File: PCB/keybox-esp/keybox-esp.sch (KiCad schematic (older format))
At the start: 3 parts, among them J1 Micro_SD_Card, U1 ESP32-WROVER

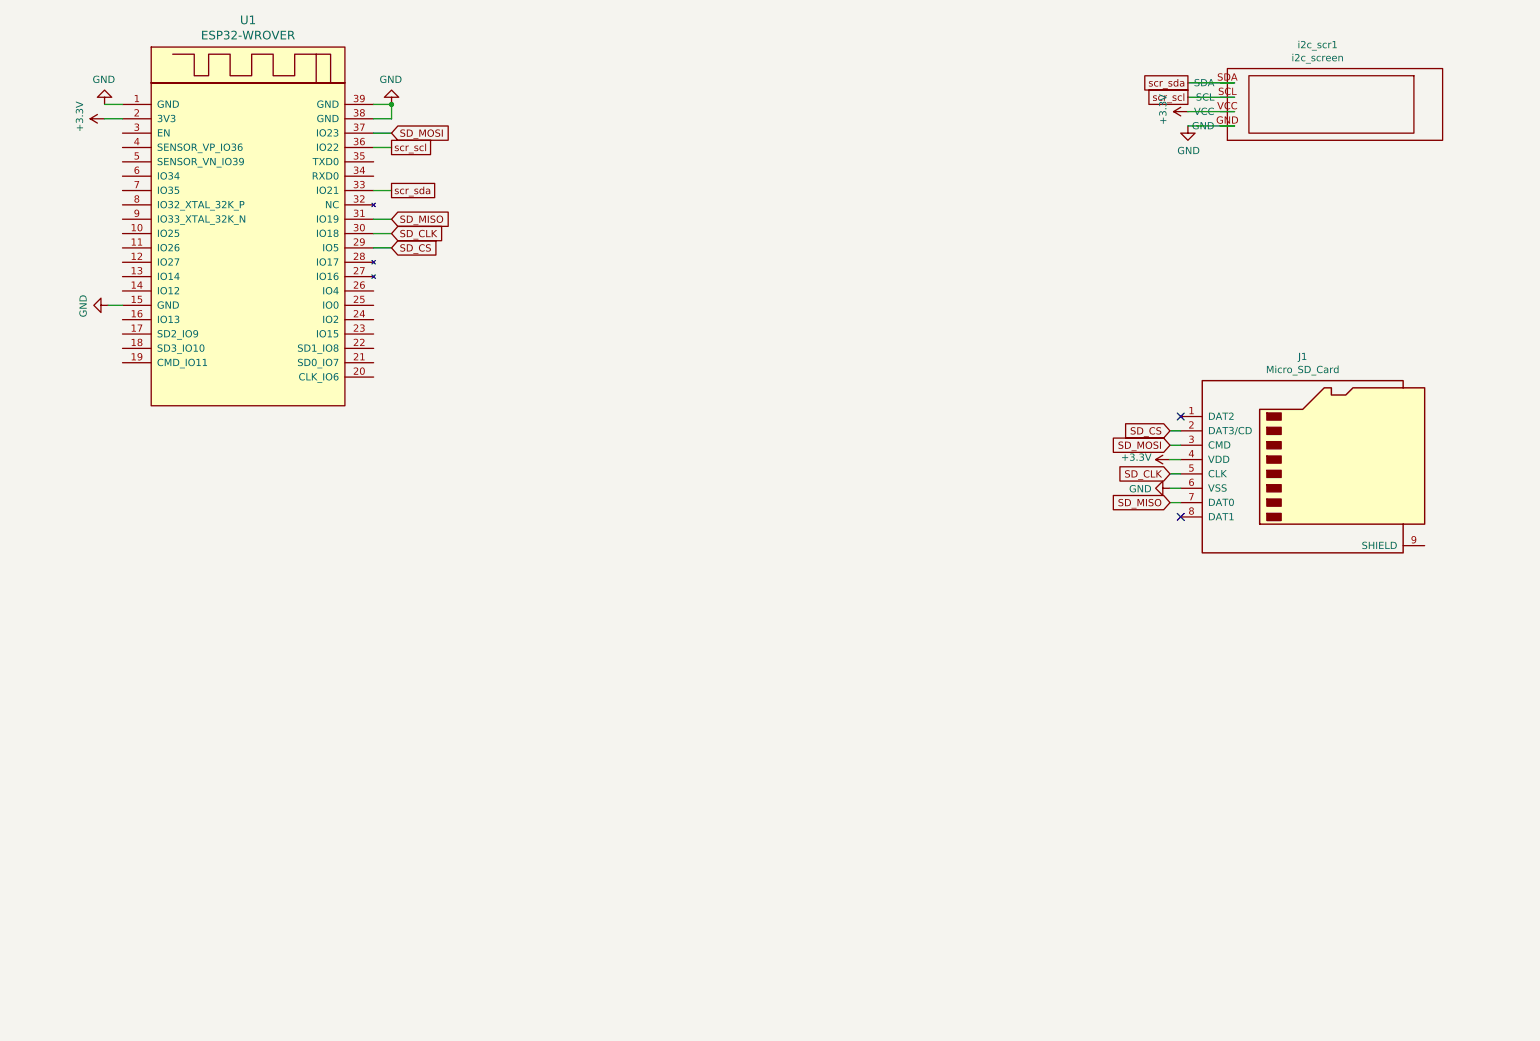
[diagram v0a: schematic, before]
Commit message: PCB sans wireing ni usb
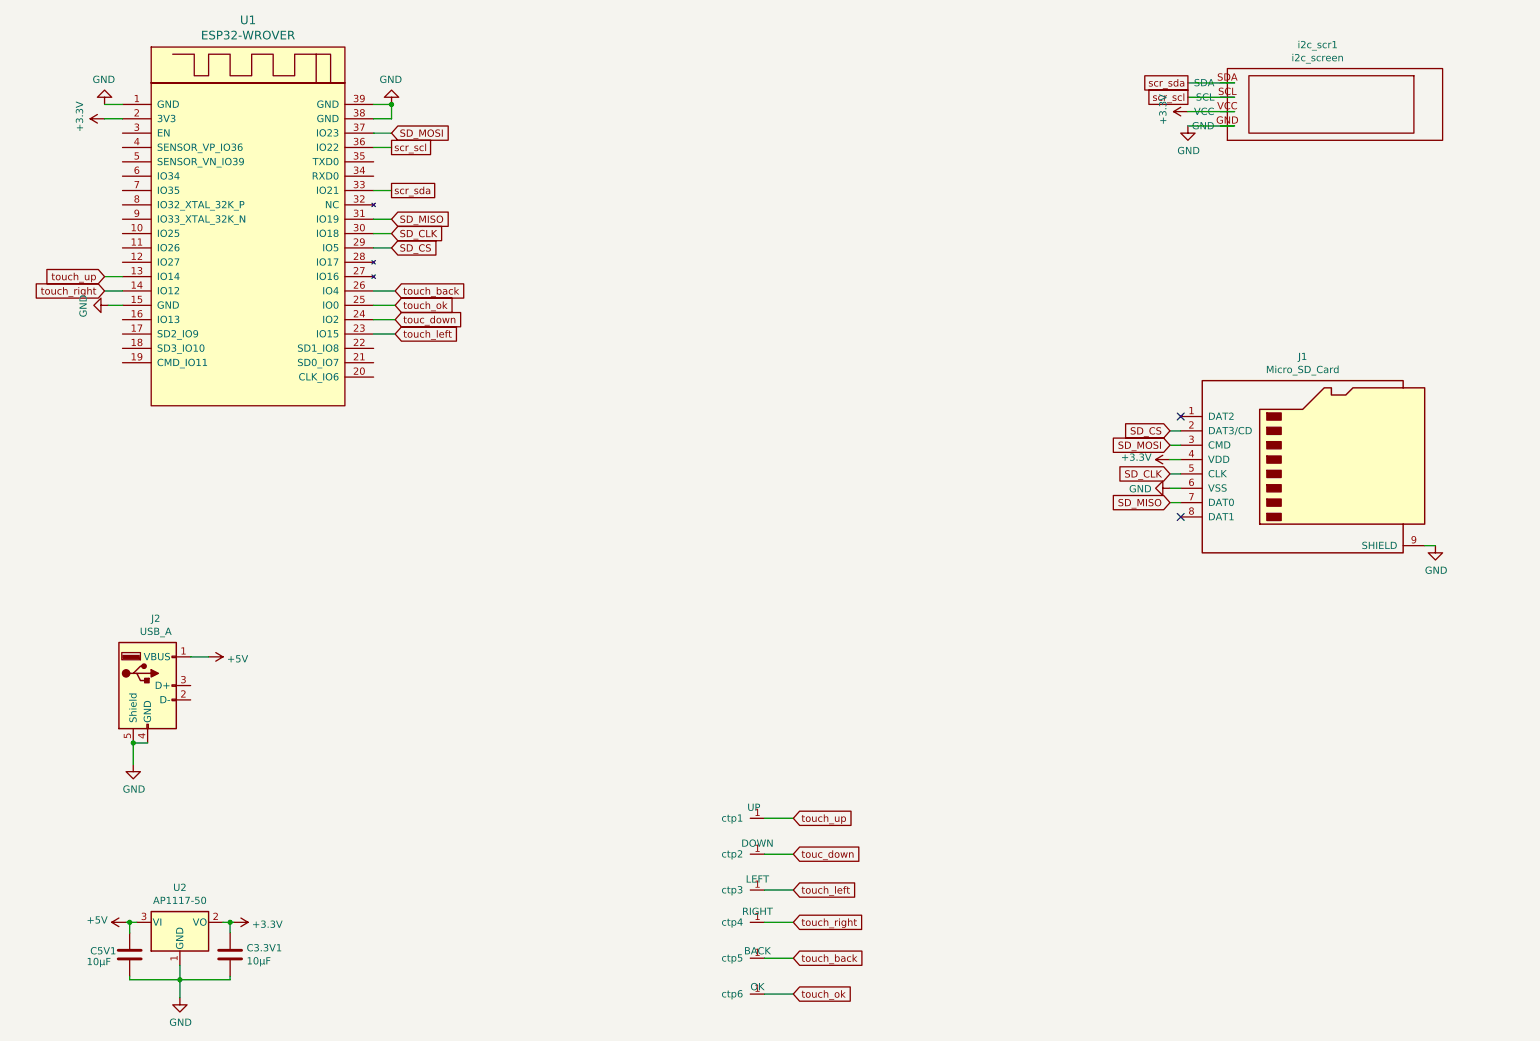
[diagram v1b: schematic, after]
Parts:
- added C3.3V1, C5V1: 10µF, AMS1117:C_1206_HandSoldering, symbol AMS1117:C
- added J2: USB_A, Connector_USB:USB3_A_Plug_Wuerth_692112030100_Horizontal, symbol Connector:USB_A
- added U2: AP1117-50, AMS1117:SOT-223-3Lead_TabPin2, symbol AMS1117:AP1117-50
- added ctp1: UP, capacitive_touch_pads:simple_pad_solder, symbol capacitive_touch_pads:capacitif_touch_pad
- added ctp2: DOWN, capacitive_touch_pads:simple_pad_solder, symbol capacitive_touch_pads:capacitif_touch_pad
- added ctp3: LEFT, capacitive_touch_pads:simple_pad_solder, symbol capacitive_touch_pads:capacitif_touch_pad
- added ctp4: RIGHT, capacitive_touch_pads:simple_pad_solder, symbol capacitive_touch_pads:capacitif_touch_pad
- added ctp5: BACK, capacitive_touch_pads:simple_pad_solder, symbol capacitive_touch_pads:capacitif_touch_pad
- added ctp6: OK, capacitive_touch_pads:simple_pad_solder, symbol capacitive_touch_pads:capacitif_touch_pad
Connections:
- net +3V3: now also C3.3V1.1, U2.2 (VO)
- net GND: now also J1.9 (SHIELD), C3.3V1.2, C5V1.2, J2.4 (GND), J2.5 (Shield), U2.1 (GND)
- net touch_up: now reaches U1.13 (IO14)
- net touch_up: now also ctp1.1 (capacitif_pad)
- net touch_right: now reaches U1.14 (IO12)
- net touch_right: now also ctp4.1 (capacitif_pad)
- net touch_left: now reaches U1.23 (IO15)
- net touch_left: now also ctp3.1 (capacitif_pad)
- net touc_down: now reaches U1.24 (IO2)
- net touc_down: now also ctp2.1 (capacitif_pad)
- net touch_ok: now reaches U1.25 (IO0)
- net touch_ok: now also ctp6.1 (capacitif_pad)
- net touch_back: now reaches U1.26 (IO4)
- net touch_back: now also ctp5.1 (capacitif_pad)
- new net +5V: C5V1.1, J2.1 (VBUS), U2.3 (VI)

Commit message: ajout du ftdi
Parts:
- added FTDI1: FTDI, Connector_Wire:SolderWirePad_1x04_P3.175mm_Drill0.8mm, symbol Connector:Conn_01x04_Female
- added flash_jumper1: flash jmp, keybox-esp:jumper_smd, symbol Connector:Conn_01x02_Male
- added rst1: rst, keybox-esp:jumper_smd, symbol Connector:Conn_01x02_Male
- renumbered ctp5 to BACK1, ctp2 to DOWN1, ctp3 to LEFT1, ctp6 to Ok1, ctp4 to RIGHT1, ctp1 to UP1
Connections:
- net +3V3: now also FTDI1.3 (Pin_3)
- net GND: now also FTDI1.4 (Pin_4), flash_jumper1.1 (Pin_1), rst1.1 (Pin_1)
- net touc_down: now also U1.12 (IO27); no longer U1.24 (IO2)
- net touch_ok: now also U1.24 (IO2); no longer U1.25 (IO0)
- net esp_reset: now reaches U1.3 (EN)
- net esp_reset: now also rst1.2 (Pin_2)
- net esp_RX: now reaches U1.34 (RXD0)
- net esp_RX: now also FTDI1.1 (Pin_1)
- net esp_TX: now reaches U1.35 (TXD0)
- net esp_TX: now also FTDI1.2 (Pin_2)
- new net flash_jmp: U1.25 (IO0), flash_jumper1.2 (Pin_2)
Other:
- moved on the sheet: J1, J2, i2c_scr1
